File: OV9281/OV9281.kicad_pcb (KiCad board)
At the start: 4 copper layers, 100 x 25 mm, 19 parts, among them IC1 TLV73328PDBVT, IC2 TLV73318PDBVT, IC3 TLV73312PDBVT, J3 WE_68715014522, U1 OV9281, U2 OV9281, Y1 Farnell_1842027, Y2 Farnell_1842027

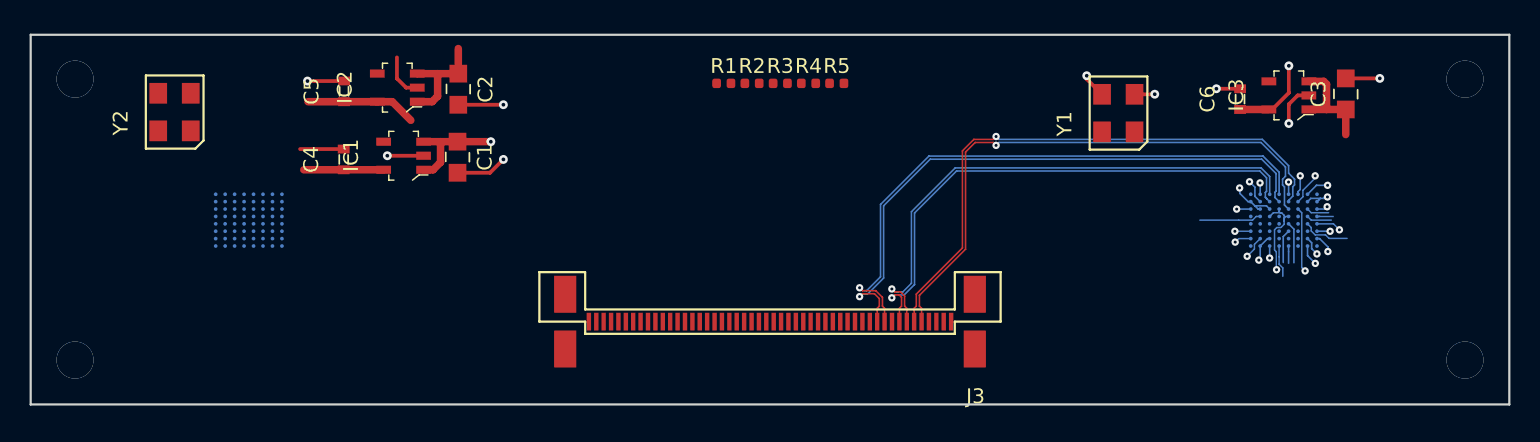
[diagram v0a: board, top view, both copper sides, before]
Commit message: Edited design rules to make bigger clearance
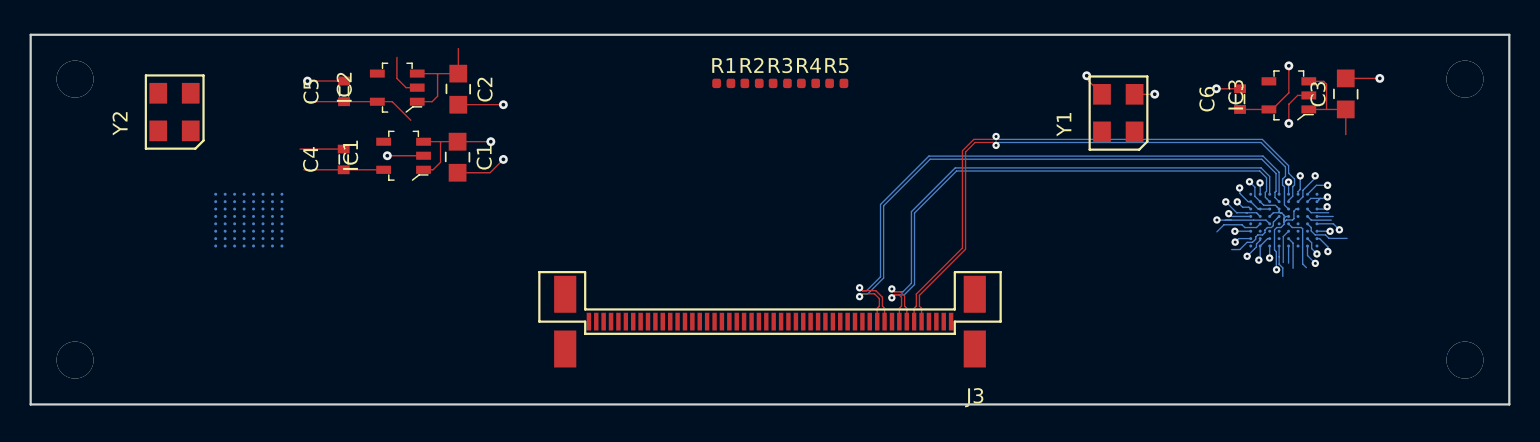
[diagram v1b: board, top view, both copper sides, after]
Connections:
- net /CLK_CAM2 renamed /M2_MCLK
- net /CLK_R renamed /M2_MCLK_M
- net /PVDD_L renamed /M1_PVDD
- net /PVDD_P renamed /M2_PVDD
- net /VH_L renamed /M1_VH
- net /VH_P renamed /M2_VH
- net /VN1_L renamed /M1_VN1
- net /VN1_P renamed /M2_VN1
- net /VN2_L renamed /M1_VN2
- net /VN2_P renamed /M2_VN2
- net /VN3_L renamed /M1_VN3
- net /VN3_P renamed /M2_VN3
- net Net-(U1-PadE1) renamed /M1_SID
- net Net-(U2-PadE1) renamed /M2_SID
- J3 pad 32: /VSYNC_1 -> /M1_VSYNC
- J3 pad 34: /VSYNC_2 -> /M2_VSYNC
- J3 pad 39: /CAM_L_SDA -> /M1_CAM_SDA
- J3 pad 40: /CAM_L_SCL -> /M1_CAM_SCL
- J3 pad 41: /CAM_R_SDA -> /M2_CAM_SDA
- J3 pad 42: /CAM_R_SCL -> /M2_CAM_SCL
- R1 pad 2: /CAM_R_SCL -> /M2_CAM_SCL
- R2 pad 2: /CAM_R_SDA -> /M2_CAM_SDA
- R3 pad 2: /CAM_L_SCL -> /M1_CAM_SCL
- R4 pad 2: /CAM_L_SDA -> /M1_CAM_SDA
- R5 pad 1: Net-(R5-Pad1) -> +3V3
- U1 pad A2: /DVDD -> /M1_DVDD
- U1 pad A3: GNDD -> /M1_DGND
- U1 pad A4: /CAM_L_SDA -> /M1_CAM_SDA_1V8
- U1 pad A5: /CAM_RST -> /CAM_NRST_1V8
- U1 pad A7: GNDD -> /M1_DGND
- U1 pad B1: /DVDD -> /M1_DVDD
- U1 pad B2: GNDD -> /M1_DGND
- U1 pad B3: /DVDD -> /M1_DVDD
- U1 pad B5: /VSYNC_1 -> /M1_VSYNC_1V8
- U1 pad B7: /DOVDD -> /M1_DOVDD
- U1 pad B8: /AVDD -> /M1_AVDD
- U1 pad C1: /AVDD -> /M1_AVDD
- U1 pad C5: /DVDD -> /M1_DVDD
- U1 pad C8: GNDA -> /M1_AGND
- U1 pad D2: GNDA -> /M1_AGND
- U1 pad D3: /DOVDD -> /M1_DOVDD
- U1 pad D8: /DVDD -> /M1_DVDD
- U1 pad E2: /CLK_L -> /M1_MCLK
- U1 pad E3: GNDD -> /M1_DGND
- U1 pad E4: /CAM_L_SCL -> /M1_CAM_SCL_1V8
- U1 pad E5: GNDD -> /M1_DGND
- U1 pad F1: GNDD -> /M1_DGND
- U1 pad F2: /DVDD -> /M1_DVDD
- U1 pad F3: /DVDD -> /M1_DVDD
- U1 pad F4: GNDD -> /M1_DGND
- U1 pad F6: GNDD -> /M1_DGND
- U1 pad F8: GNDA -> /M1_AGND
- U1 pad G1: /DVDD -> /M1_DVDD
- U1 pad G2: GNDD -> /M1_DGND
- U1 pad G6: /DVDD -> /M1_DVDD
- U1 pad G7: /AVDD -> /M1_AVDD
- U1 pad G8: /AVDD -> /M1_AVDD
- U1 pad H2: /DOVDD -> /M1_DOVDD
- U1 pad H5: /DVDD -> /M1_DVDD
- U1 pad H6: /DOVDD -> /M1_DOVDD
- U1 pad H7: GNDA -> /M1_AGND
- U2 pad A2: /DVDD -> /M2_DVDD
- U2 pad A3: GNDD -> /M2_DGND
- U2 pad A4: /CAM_R_SDA -> /M2_CAM_SDA_1V8
- U2 pad A5: /CAM_RST -> /CAM_NRST_1V8
- U2 pad A7: GNDD -> /M2_DGND
- U2 pad B1: /DVDD -> /M2_DVDD
- U2 pad B2: GNDD -> /M2_DGND
- U2 pad B3: /DVDD -> /M2_DVDD
- U2 pad B5: /VSYNC_2 -> /M2_VSYNC_1V8
- U2 pad B7: /DOVDD -> /M2_DOVDD
- U2 pad B8: /AVDD -> /M2_AVDD
- U2 pad C1: /AVDD -> /M2_AVDD
- U2 pad C5: /DVDD -> /M2_DVDD
- U2 pad C8: GNDA -> /M2_AGND
- U2 pad D2: GNDA -> /M2_AGND
- U2 pad D3: /DOVDD -> /M2_DOVDD
- U2 pad D8: /DVDD -> /M2_DVDD
- U2 pad E3: GNDD -> /M2_DGND
- U2 pad E4: /CAM_R_SCL -> /M2_CAM_SCL_1V8
- U2 pad E5: GNDD -> /M2_DGND
- U2 pad F1: GNDD -> /M2_DGND
- U2 pad F2: /DVDD -> /M2_DVDD
- U2 pad F3: /DVDD -> /M2_DVDD
- U2 pad F4: GNDD -> /M2_DGND
- U2 pad F6: GNDD -> /M2_DGND
- U2 pad F8: GNDA -> /M2_AGND
- U2 pad G1: /DVDD -> /M2_DVDD
- U2 pad G2: GNDD -> /M2_DGND
- U2 pad G6: /DVDD -> /M2_DVDD
- U2 pad G7: /AVDD -> /M2_AVDD
- U2 pad G8: /AVDD -> /M2_AVDD
- U2 pad H2: /DOVDD -> /M2_DOVDD
- U2 pad H5: /DVDD -> /M2_DVDD
- U2 pad H6: /DOVDD -> /M2_DOVDD
- U2 pad H7: GNDA -> /M2_AGND
- Y1 pad 3: /CLK_CAM1 -> /M1_MCLK
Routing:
- net GNDD: track 17.0 -> 0.00 mm, vias 7 -> 0
- net /M1_DGND: track 0.00 -> 15.9 mm, vias 0 -> 6
- net /DVDD: track 13.2 -> 0.00 mm, vias 6 -> 0
- net /M1_DVDD: track 0.00 -> 12.8 mm, vias 0 -> 6
- net /M1_DOVDD: track 0.00 -> 7.44 mm, vias 0 -> 4
- net /M1_AGND: track 0.00 -> 6.55 mm, vias 0 -> 3
- net /M1_MCLK: track 0.00 -> 4.53 mm, vias 0 -> 2
- net /M1_CAM_SCL_1V8: track 0.00 -> 4.46 mm
- net /CLK_L: track 4.18 -> 0.00 mm
- net /M1_AVDD: track 0.00 -> 4.15 mm, vias 0 -> 3
- net /AVDD: track 4.15 -> 0.00 mm, vias 3 -> 0
- net /DOVDD: track 3.38 -> 0.00 mm, vias 3 -> 0
- net GNDA: track 3.25 -> 0.00 mm, vias 3 -> 0
- net /M1_CAM_SDA_1V8: track 0.00 -> 2.16 mm
- net /CAM_L_SDA: track 2.16 -> 0.00 mm
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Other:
- net class Default: clearance 0.075 -> 0.09; trace_width 0.1 -> 0.09
- rule trace_clearance: 0.075 -> 0.09
- rule trace_min: 0.1 -> 0.09

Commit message: Defined initial component placement
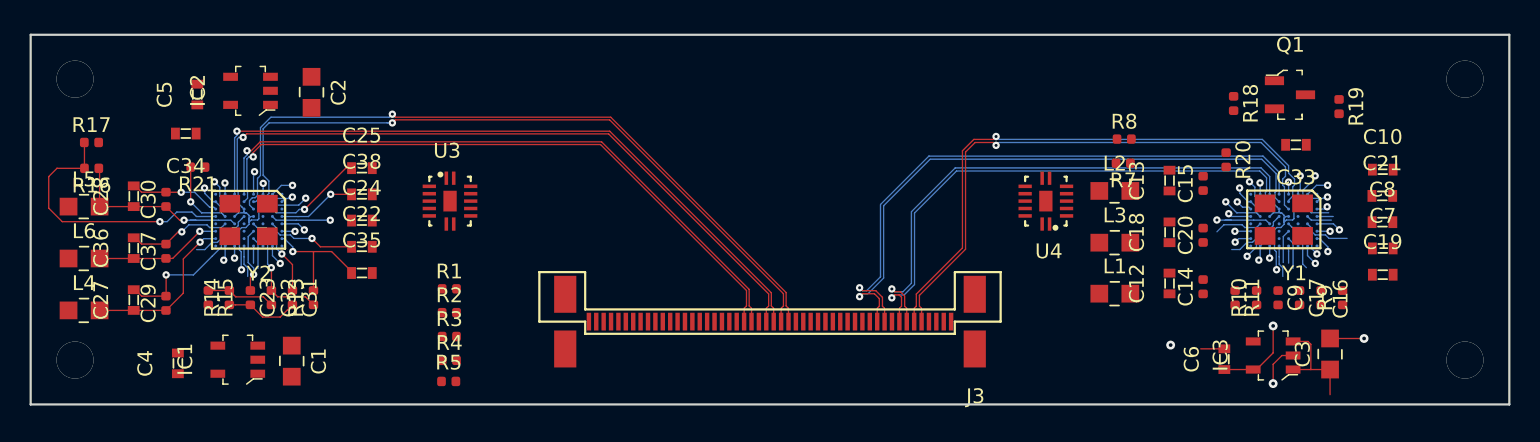
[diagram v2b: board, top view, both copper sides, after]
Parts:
- added C10: C_1u_0603, antmicro-footprints:0603-cap, F.Cu at (191.4, 109.1)
- added C12: C_1u_0603, antmicro-footprints:0603-cap, F.Cu at (177.0, 116.8)
- added C13: C_1u_0603, antmicro-footprints:0603-cap, F.Cu at (177.0, 109.9)
- added C14: C_100n_0402_6V3, antmicro-footprints:0402-cap, F.Cu at (179.3, 117.0)
- added C15: C_100n_0402_6V3, antmicro-footprints:0402-cap, F.Cu at (179.3, 110.0)
- added C16: C_100n_0402_6V3, antmicro-footprints:0402-cap, F.Cu at (187.3, 117.8)
- added C17: C_100n_0402_6V3, antmicro-footprints:0402-cap, F.Cu at (185.8, 117.8)
- added C18: C_1u_0603, antmicro-footprints:0603-cap, F.Cu at (177.0, 113.4)
- added C19: C_1u_0603, antmicro-footprints:0603-cap, F.Cu at (191.4, 116.2)
- added C20: C_100n_0402_6V3, antmicro-footprints:0402-cap, F.Cu at (179.3, 113.6)
- added C21: C_1u_0603, antmicro-footprints:0603-cap, F.Cu at (191.4, 110.9)
- added C22: C_1u_0603, antmicro-footprints:0603-cap, F.Cu at (122.4, 114.3)
- added C23: C_100n_0402_6V3, antmicro-footprints:0402-cap, F.Cu at (114.9, 117.8)
- added C24: C_1u_0603, antmicro-footprints:0603-cap, F.Cu at (122.4, 112.6)
- added C25: C_1u_0603, antmicro-footprints:0603-cap, F.Cu at (122.4, 109.0)
- added C27: C_1u_0603, antmicro-footprints:0603-cap, F.Cu at (107.0, 117.9)
- added C28: C_1u_0603, antmicro-footprints:0603-cap, F.Cu at (107.0, 110.9)
- added C29: C_100n_0402_6V3, antmicro-footprints:0402-cap, F.Cu at (109.2, 118.2)
- added C30: C_100n_0402_6V3, antmicro-footprints:0402-cap, F.Cu at (109.2, 111.1)
- added C31: C_100n_0402_6V3, antmicro-footprints:0402-cap, F.Cu at (117.7, 117.8)
- added C32: C_100n_0402_6V3, antmicro-footprints:0402-cap, F.Cu at (116.3, 117.8)
- added C33: C_1u_0603, antmicro-footprints:0603-cap, F.Cu at (185.6, 107.4)
- added C34: C_1u_0603, antmicro-footprints:0603-cap, F.Cu at (110.5, 106.7)
- added C35: C_1u_0603, antmicro-footprints:0603-cap, F.Cu at (122.4, 116.1)
- added C36: C_1u_0603, antmicro-footprints:0603-cap, F.Cu at (107.0, 114.4)
- added C37: C_100n_0402_6V3, antmicro-footprints:0402-cap, F.Cu at (109.2, 114.6)
- added C38: C_1u_0603, antmicro-footprints:0603-cap, F.Cu at (122.4, 110.8)
- added C7: C_1u_0603, antmicro-footprints:0603-cap, F.Cu at (191.4, 114.4)
- added C8: C_1u_0603, antmicro-footprints:0603-cap, F.Cu at (191.4, 112.7)
- added C9: C_100n_0402_6V3, antmicro-footprints:0402-cap, F.Cu at (184.4, 117.8)
- added L1: MLP2012S3R3MT, antmicro-footprints:0805-res, F.Cu at (173.3, 117.5)
- added L2: MLP2012S3R3MT, antmicro-footprints:0805-res, F.Cu at (173.3, 110.6)
- added L3: MLP2012S3R3MT, antmicro-footprints:0805-res, F.Cu at (173.3, 114.1)
- added L4: MLP2012S3R3MT, antmicro-footprints:0805-res, F.Cu at (103.6, 118.6)
- added L5: MLP2012S3R3MT, antmicro-footprints:0805-res, F.Cu at (103.6, 111.6)
- added L6: MLP2012S3R3MT, antmicro-footprints:0805-res, F.Cu at (103.6, 115.1)
- added Q1: BSS138AKA, antmicro-footprints:SOT-23-3, F.Cu at (185.2, 104.1)
- added R10: R_0R_0402, antmicro-footprints:0402-res, F.Cu at (182.9, 117.8)
- added R11: R_0R_0402, antmicro-footprints:0402-res, F.Cu at (181.5, 117.8)
- added R13: R_0R_0402, antmicro-footprints:0402-res, F.Cu at (119.1, 117.8)
- added R14: R_0R_0402, antmicro-footprints:0402-res, F.Cu at (113.4, 117.8)
- added R15: R_0R_0402, antmicro-footprints:0402-res, F.Cu at (112.0, 117.8)
- added R16: R_0R_0402, antmicro-footprints:0402-res, F.Cu at (104.1, 109.0)
- added R17: R_0R_0402, antmicro-footprints:0402-res, F.Cu at (104.1, 107.3)
- added R18: R_10k_0402, antmicro-footprints:0402-res, F.Cu at (181.4, 104.6)
- added R19: R_2k_0402, antmicro-footprints:0402-res, F.Cu at (188.5, 104.9)
- added R20: R_0R_0402, antmicro-footprints:0402-res, F.Cu at (180.8, 108.5)
- added R21: R_0R_0402, antmicro-footprints:0402-res, F.Cu at (111.3, 109.0)
- added R7: R_0R_0402, antmicro-footprints:0402-res, F.Cu at (173.9, 108.7)
- added R8: R_0R_0402, antmicro-footprints:0402-res, F.Cu at (174.0, 107.1)
- added R9: R_0R_0402, antmicro-footprints:0402-res, F.Cu at (188.7, 117.8)
- added U3: NTS0104BQ, antmicro-footprints:QDHVQFN14, F.Cu at (128.4, 111.2)
- added U4: NTB0104BQ, antmicro-footprints:QDHVQFN14, F.Cu at (168.7, 111.2)
- moved R5 33.1 mm to (128.3, 123.4)
- moved R4 30.7 mm to (128.3, 122.0)
- moved R3 28.2 mm to (128.3, 120.4)
- moved R2 25.7 mm to (128.3, 118.8)
- moved R1 23.2 mm to (128.3, 117.2)
- moved C1 17.8 mm to (117.7, 122.1)
- moved C4 17.8 mm to (110.0, 122.2)
- moved IC1 17.8 mm to (114.0, 122.0)
- moved C3 17.6 mm to (187.9, 121.6)
- moved IC3 17.6 mm to (184.0, 121.7)
- moved C6 17.6 mm to (180.7, 121.9)
- moved Y1 13.1 mm to (185.1, 112.3), turned to 180 degrees
- moved C5 9.93 mm to (111.3, 104.0)
- moved IC2 9.93 mm to (114.9, 103.8)
- moved C2 9.93 mm to (119.0, 103.9)
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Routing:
- net /CAM_R_D1_N: track 0.00 -> 49.0 mm, vias 0 -> 1
- net /CAM_R_D1_P: track 0.00 -> 48.1 mm, vias 0 -> 1
- net /CAM_R_D0_N: track 0.00 -> 47.0 mm, vias 0 -> 1
- net /CAM_R_D0_P: track 0.00 -> 46.9 mm, vias 0 -> 1
- net /CAM_R_CLK_N: track 0.00 -> 43.6 mm, vias 0 -> 1
- net /CAM_R_CLK_P: track 0.00 -> 43.6 mm, vias 0 -> 1
- net /M2_DGND: track 0.00 -> 33.3 mm, vias 0 -> 6
- net /M2_DVDD: track 0.00 -> 26.7 mm, vias 0 -> 7
- net /M2_AVDD: track 0.00 -> 18.9 mm, vias 0 -> 3
- net GND: track 25.6 -> 6.80 mm, vias 8 -> 3
- net /M2_SID: track 0.00 -> 18.6 mm, vias 0 -> 1
- net /M2_DOVDD: track 0.00 -> 18.5 mm, vias 0 -> 4
- net +3V3: track 22.0 -> 7.19 mm, vias 1 -> 0
- net /M2_AGND: track 0.00 -> 14.3 mm, vias 0 -> 3
- net /M2_PVDD: track 0.00 -> 8.61 mm, vias 0 -> 1
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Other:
- net class Default: clearance 0.09 -> 0.1; trace_width 0.09 -> 0.1
- rule trace_clearance: 0.09 -> 0.1

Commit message: PCB routing
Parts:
- moved R21 2.38 mm to (109.1, 108.2), turned to 0 degrees
- moved R20 1.62 mm to (179.6, 107.5), turned to 0 degrees
- moved U4 0.64 mm to (168.3, 111.8)
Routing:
- net /CAM_NRST_1V8: track 2.32 -> 126.5 mm, vias 0 -> 2
- net /M2_MCLK_M: track 5.18 -> 93.2 mm, vias 1 -> 3
- net /M2_VSYNC_1V8: track 2.14 -> 72.0 mm, vias 0 -> 3
- net /M1_CAM_SDA_1V8: track 2.16 -> 69.6 mm, vias 0 -> 3
- net +2V8: track 0.00 -> 64.7 mm, vias 0 -> 3
- net /M1_CAM_SCL_1V8: track 4.46 -> 66.4 mm, vias 0 -> 3
- net GND: track 6.80 -> 65.0 mm, vias 3 -> 22
- net +1V8: track 0.00 -> 51.2 mm, vias 0 -> 11
- net /M1_AVDD: track 4.15 -> 43.2 mm, vias 3 -> 4
- net /M1_CAM_SDA: track 0.00 -> 36.0 mm
- net +3V3: track 7.19 -> 42.9 mm, vias 0 -> 12
- net /M1_CAM_SCL: track 0.00 -> 35.1 mm
- net /M2_CAM_SDA: track 0.00 -> 34.2 mm
- net /M2_CAM_SCL: track 0.00 -> 33.3 mm
- net /M1_DOVDD: track 7.44 -> 37.1 mm, vias 4 -> 9
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- added copper zone on In2.Cu, net +1V2
- added copper zone on In2.Cu, net +1V8
- added copper zone on In2.Cu, net +2V8
- added copper zone on In2.Cu, net +3V3
- added copper zone on In1.Cu, net /M1_AGND
- added copper zone on In1.Cu, net /M1_DGND
- added copper zone on In2.Cu, net /M1_DOVDD
- added copper zone on In2.Cu, net /M1_DVDD
- added copper zone on In1.Cu, net /M2_AGND
- added copper zone on In1.Cu, net /M2_DGND
- added copper zone on In2.Cu, net /M2_DOVDD
- added copper zone on In2.Cu, net /M2_DVDD
- removed copper zone on In2.Cu, net GND
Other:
- net class Default: trace_width 0.1 -> 0.15; via_dia 0.5 -> 0.55; via_drill 0.2 -> 0.15
- net class Supply added: clearance 0.1, trace_width 0.254, via_dia 0.55, via_drill 0.15
- rule trace_min: 0.09 -> 0.1

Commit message: PCB ready for manufacturing
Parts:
- added MP1: PCB_Spacer_M2, antmicro-footprints:9774030243R, F.Cu at (103.0, 122.0)
- added MP2: PCB_Spacer_M2, antmicro-footprints:9774030243R, F.Cu at (196.9, 103.0)
- added MP3: PCB_Spacer_M2, antmicro-footprints:9774030243R, F.Cu at (103.0, 103.0)
- added MP4: PCB_Spacer_M2, antmicro-footprints:9774030243R, F.Cu at (196.9, 122.0)
- added N1: antmicro_logo, antmicro-footprints:antmicro-logo_scaled_20mm, B.Cu at (150.0, 108.7)
- moved C35 8.04 mm to (119.7, 108.6)
- moved L4 0.89 mm to (103.6, 117.8)
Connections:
- U1 pad E6: Net-(U1-PadE6) -> /M1_DGND
- U2 pad E6: Net-(U2-PadE6) -> /M2_DGND
- U4 pad 11: /M2_VSYNC -> /CAM_RST
- U4 pad 12: /CAM_RST -> /M2_VSYNC
- U4 pad 3: /CAM_RST_1V8 -> /M2_VSYNC_1V8
- U4 pad 4: /M2_VSYNC_1V8 -> /CAM_RST_1V8
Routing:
- net +2V8: track 64.7 -> 41.2 mm, vias 3 -> 2
- net /M2_DVDD: track 29.9 -> 48.2 mm, vias 7 -> 9
- net /M1_DVDD: track 25.5 -> 40.4 mm, vias 7 -> 9
- net /CAM_R_CLK_P: track 43.4 -> 52.8 mm
- net /CAM_R_D1_N: track 59.5 -> 52.5 mm
- net /CAM_R_D1_P: track 59.0 -> 52.5 mm
- net /CAM_R_CLK_N: track 46.7 -> 52.8 mm
- net /M1_AVDD: track 43.2 -> 49.1 mm, vias 4 -> 5
- net +1V2: track 12.5 -> 17.9 mm, vias 3 -> 6
- net /CAM_R_D0_N: track 47.7 -> 52.4 mm
- net /CAM_R_D0_P: track 47.9 -> 52.3 mm
- net /M2_VSYNC_1V8: track 72.0 -> 75.0 mm
- net GND: track 65.0 -> 62.8 mm, vias 22 -> 23
- net /CAM_L_D0_P: track 41.8 -> 39.7 mm
- net /M2_AVDD: track 43.5 -> 45.6 mm
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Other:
- net class Default: trace_width 0.15 -> 0.1
- board text added: "."
- board text added: "50"
- board text added: "OV9281 Dual Camera Board"
- board text added: "Rev.1.0 09/2019"

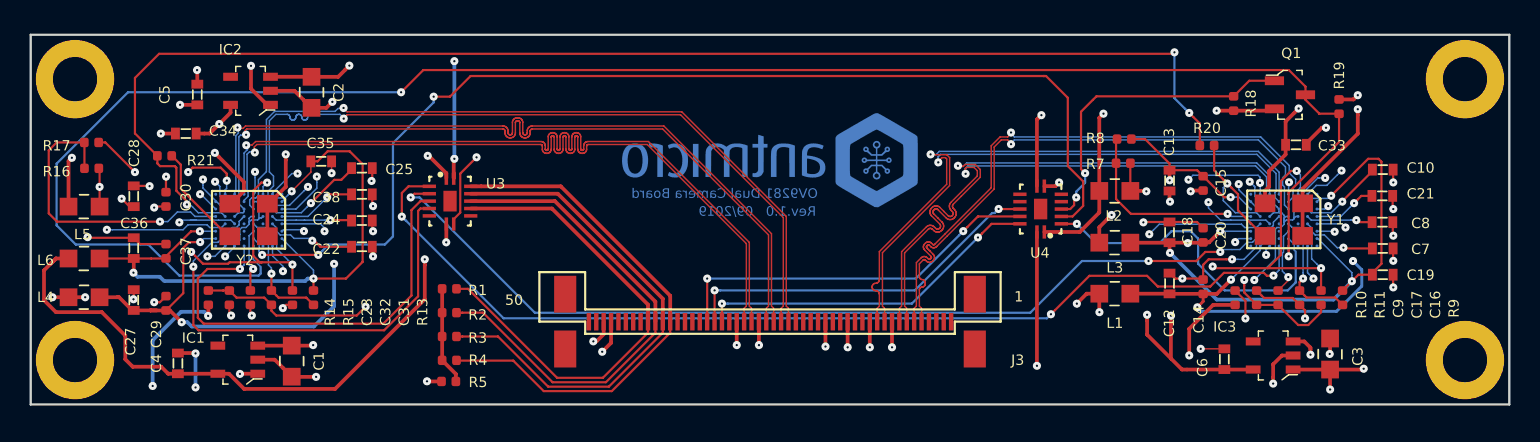
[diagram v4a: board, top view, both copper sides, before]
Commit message: Added mounting holes for lenses
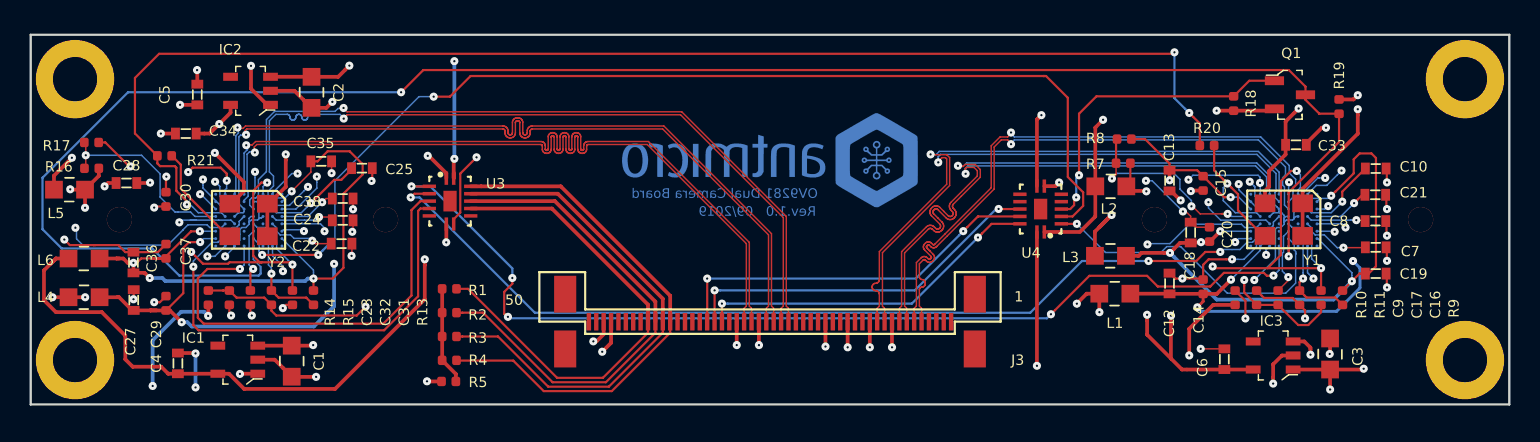
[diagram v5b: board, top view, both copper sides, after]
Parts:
- added REF**: Camera_Lens, antmicro-footprints:Camera_Lens, B.Cu at (185.0, 112.5)
- added REF**: Camera_Lens, antmicro-footprints:Camera_Lens, B.Cu at (115.0, 112.5)
- moved L5 1.51 mm to (102.6, 110.5)
- moved C18 1.43 mm to (178.4, 113.4)
- moved C22 1.39 mm to (121.0, 114.1)
- moved C38 1.33 mm to (121.1, 111.1)
- moved C24 1.30 mm to (121.1, 112.5)
- moved C28 1.02 mm to (106.5, 110.0), turned to 0 degrees
- moved C36 0.97 mm to (107.0, 115.4)
- moved L3 0.94 mm to (173.0, 115.0)
- moved C10 0.48 mm to (191.0, 109.0)
- moved C19 0.48 mm to (191.0, 116.2)
- moved C21 0.48 mm to (190.9, 110.8)
- moved C7 0.48 mm to (191.0, 114.4)
- moved C8 0.48 mm to (190.9, 112.6)
- moved C20 0.44 mm to (179.7, 113.5)
- moved L2 0.41 mm to (173.1, 110.2)
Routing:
- net /M2_SID: track 20.6 -> 13.3 mm
- net /M2_AGND: track 37.2 -> 42.7 mm
- net /M1_AVDD: track 49.1 -> 44.8 mm
- net +2V8: track 41.2 -> 43.4 mm
- net /M1_AGND: track 28.2 -> 30.0 mm, vias 12 -> 13
- net /M2_VN1: track 6.13 -> 4.58 mm
- net /CAM_NRST_1V8: track 124.4 -> 125.9 mm
- net /M2_AVDD: track 45.6 -> 47.0 mm, vias 4 -> 5
- net /M2_DOVDD: track 31.9 -> 33.2 mm, vias 9 -> 10
- net /M2_VH: track 5.32 -> 4.00 mm
- net +1V8: track 50.8 -> 49.6 mm
- net /M2_VN2: track 5.46 -> 4.33 mm
- net /M1_VSYNC_1V8: track 22.8 -> 21.7 mm
- net /M2_VSYNC_1V8: track 75.0 -> 73.9 mm
- net /M1_VH: track 4.29 -> 3.58 mm
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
